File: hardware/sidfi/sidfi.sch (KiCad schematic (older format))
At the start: 39 parts, among them J1 ICSP, J2 SD_CARD, J3 USB_B, J4 AUDIO_OUT, J5 LCD_KEYS, Q1 2N3904, U1 74HCT164, U2 74HCT164, U3 MCP1700-3302E_TO92, U4 74HC148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

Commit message: PCB--WIP
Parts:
- J2: footprint Connector_PinHeader_2.54mm:PinHeader_1x09_P2.54mm_Horizontal -> Connector_PinSocket_2.54mm:PinSocket_1x09_P2.54mm_Horizontal
- J3: footprint (none) -> sidfi:CUI_UJ2-BH-1-TH
- J4: footprint (none) -> sidfi:CUI_SJ1-3523NG
- Q1: footprint Package_TO_SOT_THT:TO-92_Inline -> Package_TO_SOT_THT:TO-92_HandSolder
- U6: footprint Package_DIP:DIP-28_W7.62mm -> Package_DIP:DIP-28_W15.24mm
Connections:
- net GND: now also J2.3 (Pin_3); no longer J2.7 (Pin_7)
- net SD_CARD_CD: now also J2.1 (Pin_1); no longer J2.9 (Pin_9)
- net SD_CARD_CS: now also J2.4 (Pin_4); no longer J2.6 (Pin_6)
- net SD_CARD_SCK: now also J2.5 (Pin_5); no longer J2.3 (Pin_3)
- net SD_CARD_SDI: now also J2.6 (Pin_6), U5.14 (TMS/RPB5/USBID/RB5); no longer J2.4 (Pin_4), U5.17 (TCK/RPB8/SCL1/CTED10/PMD4/RB8)
- net SD_CARD_SDO: now also J2.7 (Pin_7), U5.17 (TCK/RPB8/SCL1/CTED10/PMD4/RB8); no longer J2.5 (Pin_5), U5.14 (TMS/RPB5/USBID/RB5)
- net VCC: now also J2.9 (Pin_9); no longer J2.1 (Pin_1)
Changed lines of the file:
@@
 F 0 "U6" H 8200 7215 50  0000 C CNN
 F 1 "MOS6581" H 8200 7124 50  0000 C CNN
-F 2 "Package_DIP:DIP-28_W7.62mm" H 8300 6550 50  0001 C CNN
+F 2 "Package_DIP:DIP-28_W15.24mm" H 8300 6550 50  0001 C CNN
 F 3 "" H 8300 6550 50  0001 C CNN
 	1    8200 6550
@@
 Wire Wire Line
 	8700 2800 8850 2800
+Text GLabel 8850 2500 2    50   Input ~ 0
+SD_CARD_SDO
 Text GLabel 8850 2300 2    50   Input ~ 0
-SD_CARD_SDO
-Text GLabel 8850 2500 2    50   Input ~ 0
 SD_CARD_SDI
 Text GLabel 8850 3000 2    50   Input ~ 0
@@
 F 0 "J4" H 5132 10525 50  0000 C CNN
 F 1 "AUDIO_OUT" H 5132 10434 50  0000 C CNN
-F 2 "" H 5100 10200 50  0001 C CNN
+F 2 "sidfi:CUI_SJ1-3523NG" H 5100 10200 50  0001 C CNN
 F 3 "~" H 5100 10200 50  0001 C CNN
 	1    5100 10200
@@
 F 0 "J2" H 15130 6192 50  0000 L CNN
 F 1 "SD_CARD" H 15130 6101 50  0000 L CNN
-F 2 "Connector_PinHeader_2.54mm:PinHeader_1x09_P2.54mm_Horizontal" H 15050 6150 50  0001 C CNN
+F 2 "Connector_PinSocket_2.54mm:PinSocket_1x09_P2.54mm_Horizontal" H 15050 6150 50  0001 C CNN
 F 3 "~" H 15050 6150 50  0001 C CNN
 	1    15050 6150
@@
 	1    0    0    -1
 $EndComp
-Wire Wire Line
-	14850 5750 14700 5750
-Wire Wire Line
-	14700 5750 14700 5650
 $Comp
 L power:GND #PWR04
 U 1 1 608A8824
-P 14700 6700
-F 0 "#PWR04" H 14700 6450 50  0001 C CNN
-F 1 "GND" H 14705 6527 50  0000 C CNN
-F 2 "" H 14700 6700 50  0001 C CNN
-F 3 "" H 14700 6700 50  0001 C CNN
-	1    14700 6700
-	1    0    0    -1
-$EndComp
-Wire Wire Line
-	14850 5850 14700 5850
-Wire Wire Line
-	14700 5850 14700 6350
-Text GLabel 14550 5950 0    50   Input ~ 0
+P 14600 6700
+F 0 "#PWR04" H 14600 6450 50  0001 C CNN
+F 1 "GND" H 14605 6527 50  0000 C CNN
+F 2 "" H 14600 6700 50  0001 C CNN
+F 3 "" H 14600 6700 50  0001 C CNN
+	1    14600 6700
+	1    0    0    -1
+$EndComp
+Text GLabel 14450 6150 0    50   Input ~ 0
 SD_CARD_SCK
-Wire Wire Line
-	14850 5950 14550 5950
-Text GLabel 14550 6050 0    50   Input ~ 0
+Text GLabel 14450 6250 0    50   Input ~ 0
 SD_CARD_SDI
-Wire Wire Line
-	14550 6050 14850 6050
-Text GLabel 14550 6150 0    50   Input ~ 0
+Text GLabel 14450 6350 0    50   Input ~ 0
 SD_CARD_SDO
-Wire Wire Line
-	14850 6150 14550 6150
-Text GLabel 14550 6250 0    50   Input ~ 0
+Text GLabel 14450 6050 0    50   Input ~ 0
 SD_CARD_CS
-Wire Wire Line
-	14550 6250 14850 6250
-Wire Wire Line
-	14850 6350 14700 6350
-Connection ~ 14700 6350
-Wire Wire Line
-	14700 6350 14700 6450
-Wire Wire Line
-	14850 6450 14700 6450
-Connection ~ 14700 6450
-Wire Wire Line
-	14700 6450 14700 6700
-Text GLabel 14550 6550 0    50   Input ~ 0
+Text GLabel 14450 5750 0    50   Input ~ 0
 SD_CARD_CD
-Wire Wire Line
-	14550 6550 14850 6550
 Wire Wire Line
 	14600 4250 14850 4250
@@
 F 0 "Q1" H 3490 9846 50  0000 L CNN
 F 1 "2N3904" H 3490 9755 50  0000 L CNN
-F 2 "Package_TO_SOT_THT:TO-92_Inline" H 3500 9725 50  0001 L CIN
+F 2 "Package_TO_SOT_THT:TO-92_HandSolder" H 3500 9725 50  0001 L CIN
 F 3 "https://www.onsemi.com/pub/Collateral/2N3903-D.PDF" H 3300 9800 50  0001 L CNN
 	1    3300 9800
@@
 Text GLabel 15300 8500 2    50   Input ~ 0
 LCD_DC
-Text GLabel 15300 8300 2    50   Input ~ 0
-LCD_BLK
-Wire Wire Line
-	14950 8300 15300 8300
 Wire Wire Line
 	14950 8500 15300 8500
@@
 NoConn ~ 14450 7700
 NoConn ~ 14450 7600
-Text GLabel 12700 9150 2    50   Input ~ 0
-LCD_BLK
 $Comp
 L power:VCC #PWR045
 U 1 1 608D484E
-P 12600 9000
-F 0 "#PWR045" H 12600 8850 50  0001 C CNN
-F 1 "VCC" H 12617 9173 50  0000 C CNN
-F 2 "" H 12600 9000 50  0001 C CNN
-F 3 "" H 12600 9000 50  0001 C CNN
-	1    12600 9000
-	1    0    0    -1
-$EndComp
-Wire Wire Line
-	12600 9000 12600 9150
-Wire Wire Line
-	12600 9150 12700 9150
+P 15250 7350
+F 0 "#PWR045" H 15250 7200 50  0001 C CNN
+F 1 "VCC" H 15267 7523 50  0000 C CNN
+F 2 "" H 15250 7350 50  0001 C CNN
+F 3 "" H 15250 7350 50  0001 C CNN
+	1    15250 7350
+	1    0    0    -1
+$EndComp
 Text GLabel 8850 2100 2    50   Input ~ 0
 LCD_RESET
@@
 F 0 "J3" H 14757 2667 50  0000 C CNN
 F 1 "USB_B" H 14757 2576 50  0000 C CNN
-F 2 "" H 14850 2150 50  0001 C CNN
+F 2 "sidfi:CUI_UJ2-BH-1-TH" H 14850 2150 50  0001 C CNN
 F 3 " ~" H 14850 2150 50  0001 C CNN
 	1    14700 2200
@@
 Wire Wire Line
 	3700 6850 2700 6850
+Wire Wire Line
+	14700 5650 14700 6550
+Wire Wire Line
+	14700 6550 14850 6550
+Wire Wire Line
+	14600 6700 14600 6450
+Wire Wire Line
+	14600 6450 14850 6450
+Wire Wire Line
+	14450 5750 14850 5750
+Wire Wire Line
+	14850 5850 14600 5850
+Wire Wire Line
+	14600 5850 14600 5950
+Connection ~ 14600 6450
+Wire Wire Line
+	14850 5950 14600 5950
+Connection ~ 14600 5950
+Wire Wire Line
+	14600 5950 14600 6450
+Wire Wire Line
+	14450 6050 14850 6050
+Wire Wire Line
+	14450 6150 14850 6150
+Wire Wire Line
+	14450 6250 14850 6250
+Wire Wire Line
+	14450 6350 14850 6350
+Wire Wire Line
+	14950 8300 15250 8300
+Wire Wire Line
+	15250 7350 15250 8300
 $EndSCHEMATC

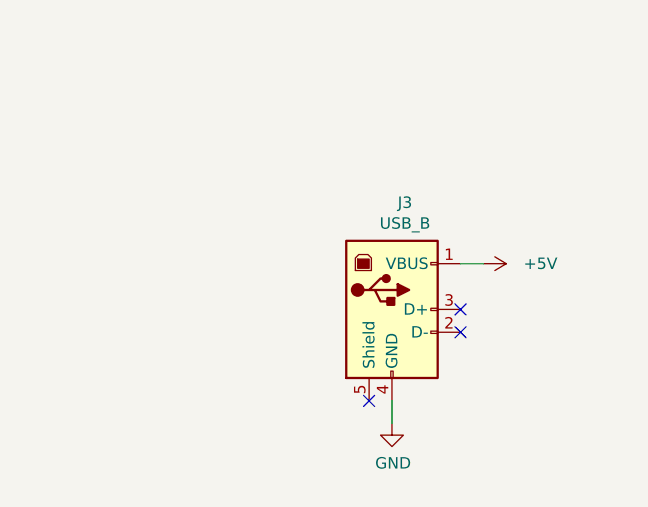
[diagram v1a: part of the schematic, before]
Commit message: Route the PCB
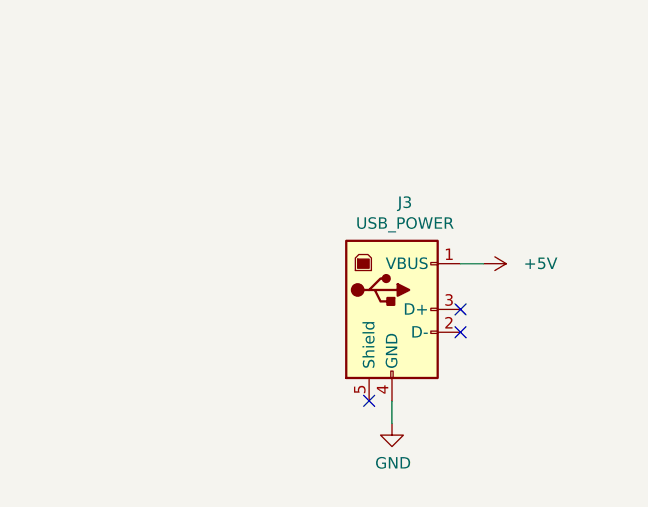
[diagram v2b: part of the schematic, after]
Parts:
- J3: value USB_B -> USB_POWER
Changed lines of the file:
@@
 P 14700 2200
 F 0 "J3" H 14757 2667 50  0000 C CNN
-F 1 "USB_B" H 14757 2576 50  0000 C CNN
+F 1 "USB_POWER" H 14757 2576 50  0000 C CNN
 F 2 "sidfi:CUI_UJ2-BH-1-TH" H 14850 2150 50  0001 C CNN
 F 3 " ~" H 14850 2150 50  0001 C CNN

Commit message: Logo. Redo PCB.
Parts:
- added J6: 5V, Connector_PinHeader_2.54mm:PinHeader_1x02_P2.54mm_Vertical, symbol Connector_Generic:Conn_01x02
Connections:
- net +5V: now also J6.1 (Pin_1)
- net GND: now also J6.2 (Pin_2); no longer J2.2 (Pin_2), J2.3 (Pin_3)
- no-connect marks 28 -> 30
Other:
- moved on the sheet: J3
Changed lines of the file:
@@
 	12500 8250 12600 8250
 Connection ~ 1050 2350
-NoConn ~ 14600 2600
-NoConn ~ 15000 2300
-NoConn ~ 15000 2200
-Wire Wire Line
-	15000 2000 15100 2000
+NoConn ~ 14600 3000
+NoConn ~ 15000 2700
+NoConn ~ 15000 2600
+Wire Wire Line
+	15000 2400 15100 2400
 $Comp
 L power:+5V #PWR014
 U 1 1 607B5683
-P 15100 2000
-F 0 "#PWR014" H 15100 1850 50  0001 C CNN
-F 1 "+5V" V 15100 2250 50  0000 C CNN
-F 2 "" H 15100 2000 50  0001 C CNN
-F 3 "" H 15100 2000 50  0001 C CNN
-	1    15100 2000
+P 15100 2400
+F 0 "#PWR014" H 15100 2250 50  0001 C CNN
+F 1 "+5V" V 15100 2650 50  0000 C CNN
+F 2 "" H 15100 2400 50  0001 C CNN
+F 3 "" H 15100 2400 50  0001 C CNN
+	1    15100 2400
 	0    1    1    0
 $EndComp
@@
 L power:GND #PWR012
 U 1 1 607B3DF7
-P 14700 2700
-F 0 "#PWR012" H 14700 2450 50  0001 C CNN
-F 1 "GND" H 14705 2527 50  0000 C CNN
-F 2 "" H 14700 2700 50  0001 C CNN
-F 3 "" H 14700 2700 50  0001 C CNN
-	1    14700 2700
+P 14700 3100
+F 0 "#PWR012" H 14700 2850 50  0001 C CNN
+F 1 "GND" H 14705 2927 50  0000 C CNN
+F 2 "" H 14700 3100 50  0001 C CNN
+F 3 "" H 14700 3100 50  0001 C CNN
+	1    14700 3100
 	1    0    0    -1
 $EndComp
@@
 L Connector:USB_B J3
 U 1 1 607AE78D
-P 14700 2200
-F 0 "J3" H 14757 2667 50  0000 C CNN
-F 1 "USB_POWER" H 14757 2576 50  0000 C CNN
-F 2 "sidfi:CUI_UJ2-BH-1-TH" H 14850 2150 50  0001 C CNN
-F 3 " ~" H 14850 2150 50  0001 C CNN
-	1    14700 2200
+P 14700 2600
+F 0 "J3" H 14757 3067 50  0000 C CNN
+F 1 "USB_POWER" H 14757 2976 50  0000 C CNN
+F 2 "sidfi:CUI_UJ2-BH-1-TH" H 14850 2550 50  0001 C CNN
+F 3 " ~" H 14850 2550 50  0001 C CNN
+	1    14700 2600
 	1    0    0    -1
 $EndComp
@@
 	1050 2350 1050 1950
 Wire Wire Line
-	14700 2600 14700 2700
+	14700 3000 14700 3100
 Connection ~ 12950 7950
 Wire Wire Line
@@
 	14450 5750 14850 5750
 Wire Wire Line
-	14850 5850 14600 5850
-Wire Wire Line
-	14600 5850 14600 5950
-Connection ~ 14600 6450
-Wire Wire Line
-	14850 5950 14600 5950
-Connection ~ 14600 5950
-Wire Wire Line
-	14600 5950 14600 6450
-Wire Wire Line
 	14450 6050 14850 6050
 Wire Wire Line
@@
 Wire Wire Line
 	15250 7350 15250 8300
+NoConn ~ 14850 5850
+NoConn ~ 14850 5950
+$Comp
+L Connector_Generic:Conn_01x02 J6
+U 1 1 6084CCCA
+P 15000 1200
+F 0 "J6" H 15080 1192 50  0000 L CNN
+F 1 "5V" H 15080 1101 50  0000 L CNN
+F 2 "Connector_PinHeader_2.54mm:PinHeader_1x02_P2.54mm_Vertical" H 15000 1200 50  0001 C CNN
+F 3 "~" H 15000 1200 50  0001 C CNN
+	1    15000 1200
+	1    0    0    -1
+$EndComp
+$Comp
+L power:+5V #PWR042
+U 1 1 608612A7
+P 14700 950
+F 0 "#PWR042" H 14700 800 50  0001 C CNN
+F 1 "+5V" H 14715 1123 50  0000 C CNN
+F 2 "" H 14700 950 50  0001 C CNN
+F 3 "" H 14700 950 50  0001 C CNN
+	1    14700 950
+	1    0    0    -1
+$EndComp
+$Comp
+L power:GND #PWR048
+U 1 1 60861769
+P 14700 1500
+F 0 "#PWR048" H 14700 1250 50  0001 C CNN
+F 1 "GND" H 14705 1327 50  0000 C CNN
+F 2 "" H 14700 1500 50  0001 C CNN
+F 3 "" H 14700 1500 50  0001 C CNN
+	1    14700 1500
+	1    0    0    -1
+$EndComp
+Wire Wire Line
+	14800 1300 14700 1300
+Wire Wire Line
+	14700 1300 14700 1500
+Wire Wire Line
+	14800 1200 14700 1200
+Wire Wire Line
+	14700 1200 14700 950
+$Comp
+L logo:LOGO #G1
+U 1 1 609A2754
+P 12850 10250
+F 0 "#G1" H 12850 10030 60  0001 C CNN
+F 1 "LOGO" H 12850 10470 60  0001 C CNN
+F 2 "" H 12850 10250 50  0001 C CNN
+F 3 "" H 12850 10250 50  0001 C CNN
+	1    12850 10250
+	1    0    0    -1
+$EndComp
 $EndSCHEMATC
